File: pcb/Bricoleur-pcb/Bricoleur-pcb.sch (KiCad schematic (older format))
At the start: 29 parts, among them J1 USB_B_Micro, SW2 SW_Push, U11 SW_DP3T, U2 PYNQ-Shield-Bricoleur-pcb-cac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, U5 Arducam-OV5642, U6 Arducam-OV5642, U7 EFM32GG980, U8 UART_BOOT, U9 IP4220CZ6

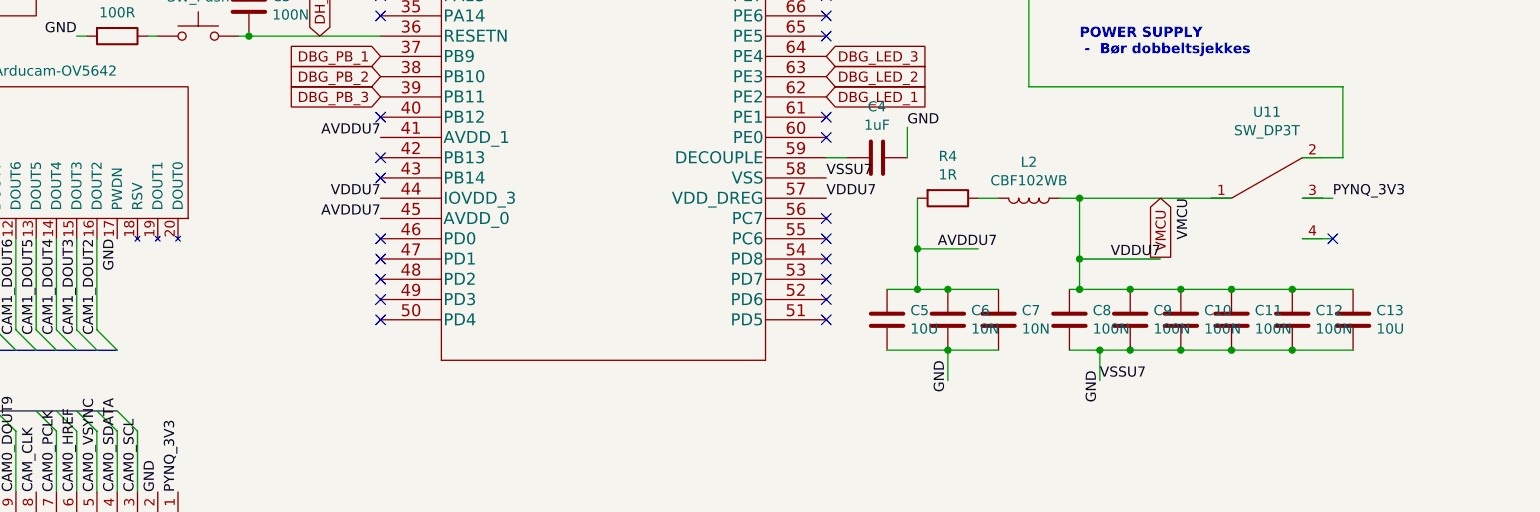
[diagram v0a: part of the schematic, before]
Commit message: Power and clock networks ready (probably).
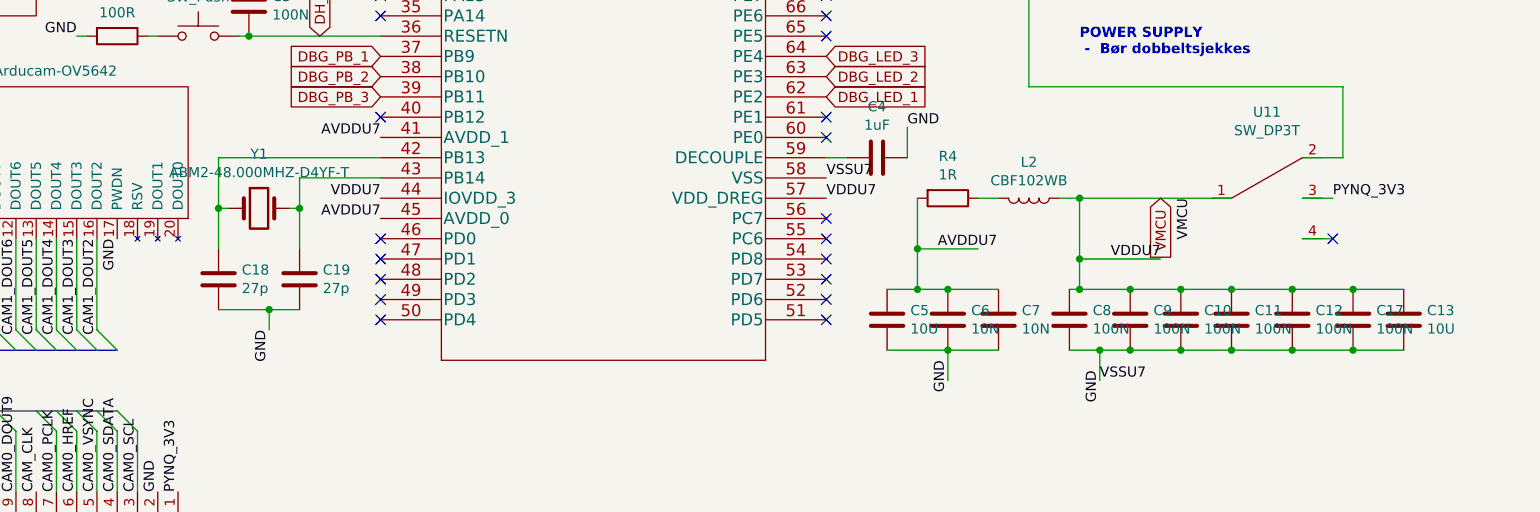
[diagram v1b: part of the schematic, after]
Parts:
- added C17: 100N, Capacitor_SMD:C_0402_1005Metric, symbol Device:C
- added C18, C19: 27p, Capacitor_SMD:C_0402_1005Metric, symbol Device:C
- added Y1: ABM2-48.000MHZ-D4YF-T, XTAL:XTAL, symbol Device:Crystal
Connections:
- net GND: now also C17.2, C18.2, C19.2
- net VMCU: now also C17.1
- net at U7.42 (PB13): now also C18.1, Y1.1
- net at U7.43 (PB14): now also C19.1, Y1.2
- no-connect marks 83 -> 81
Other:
- moved on the sheet: C13
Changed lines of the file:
@@
 L Device:C C13
 U 1 1 5BA5CA48
-P 10950 6100
-F 0 "C13" H 11065 6146 50  0000 L CNN
-F 1 "10U" H 11065 6055 50  0000 L CNN
-F 2 "Capacitor_SMD:C_0805_2012Metric" H 10988 5950 50  0001 C CNN
-F 3 "~" H 10950 6100 50  0001 C CNN
-	1    10950 6100
+P 11200 6100
+F 0 "C13" H 11315 6146 50  0000 L CNN
+F 1 "10U" H 11315 6055 50  0000 L CNN
+F 2 "Capacitor_SMD:C_0805_2012Metric" H 11238 5950 50  0001 C CNN
+F 3 "~" H 11200 6100 50  0001 C CNN
+	1    11200 6100
 	1    0    0    -1
 $EndComp
@@
 NoConn ~ 6150 4600
 NoConn ~ 6150 5100
-NoConn ~ 6150 5300
-NoConn ~ 6150 5400
 NoConn ~ 6150 5700
 NoConn ~ 6150 5800
@@
 Wire Wire Line
 	9750 2750 9300 2750
-Wire Wire Line
-	2350 5200 2950 5200
-Wire Wire Line
-	8350 4000 9050 4000
-Wire Wire Line
-	2350 5700 2950 5700
-Wire Bus Line
-	8950 2700 8950 4200
-Wire Bus Line
-	3000 650  3000 4750
-Wire Bus Line
-	3050 4750 3050 5650
-Wire Bus Line
-	2900 6550 4850 6550
-Wire Bus Line
-	2900 5100 2900 6550
-Wire Bus Line
-	3000 6250 4850 6250
-Wire Bus Line
-	2900 3600 2900 4850
 Text Label 10050 1750 0    50   ~ 0
 USB_D-
 Text Label 10050 1850 0    50   ~ 0
 USB_D+
+$Comp
+L Device:C C17
+U 1 1 5BB181A5
+P 10950 6100
+F 0 "C17" H 11065 6146 50  0000 L CNN
+F 1 "100N" H 11065 6055 50  0000 L CNN
+F 2 "Capacitor_SMD:C_0402_1005Metric" H 10988 5950 50  0001 C CNN
+F 3 "~" H 10950 6100 50  0001 C CNN
+	1    10950 6100
+	1    0    0    -1
+$EndComp
+Wire Wire Line
+	11200 5950 10950 5950
+Connection ~ 10950 5950
+Wire Wire Line
+	11200 6250 10950 6250
+Connection ~ 10950 6250
+$Comp
+L Device:Crystal Y1
+U 1 1 5BB326B9
+P 5550 5550
+F 0 "Y1" H 5550 5818 50  0000 C CNN
+F 1 "ABM2-48.000MHZ-D4YF-T" H 5550 5727 50  0000 C CNN
+F 2 "XTAL:XTAL" H 5550 5550 50  0001 C CNN
+F 3 "~" H 5550 5550 50  0001 C CNN
+	1    5550 5550
+	1    0    0    -1
+$EndComp
+Wire Wire Line
+	5750 5750 5750 5550
+Wire Wire Line
+	5750 5550 5700 5550
+Wire Wire Line
+	5350 5750 5350 5550
+Wire Wire Line
+	5350 5550 5400 5550
+Text Label 5600 6150 3    50   ~ 0
+GND
+Wire Wire Line
+	5600 6150 5600 6050
+Wire Wire Line
+	5600 6050 5350 6050
+Wire Wire Line
+	5600 6050 5750 6050
+Connection ~ 5600 6050
+Wire Wire Line
+	5750 5400 5750 5550
+Connection ~ 5750 5550
+Wire Wire Line
+	5350 5300 5350 5550
+Connection ~ 5350 5550
+$Comp
+L Device:C C18
+U 1 1 5BB1AE61
+P 5350 5900
+F 0 "C18" H 5465 5946 50  0000 L CNN
+F 1 "27p" H 5465 5855 50  0000 L CNN
+F 2 "Capacitor_SMD:C_0402_1005Metric" H 5388 5750 50  0001 C CNN
+F 3 "~" H 5350 5900 50  0001 C CNN
+	1    5350 5900
+	1    0    0    -1
+$EndComp
+$Comp
+L Device:C C19
+U 1 1 5BB1B027
+P 5750 5900
+F 0 "C19" H 5865 5946 50  0000 L CNN
+F 1 "27p" H 5865 5855 50  0000 L CNN
+F 2 "Capacitor_SMD:C_0402_1005Metric" H 5788 5750 50  0001 C CNN
+F 3 "~" H 5750 5900 50  0001 C CNN
+	1    5750 5900
+	1    0    0    -1
+$EndComp
+Wire Wire Line
+	6150 5400 5750 5400
+Wire Wire Line
+	5350 5300 6150 5300
+Wire Wire Line
+	2350 5700 2950 5700
+Wire Wire Line
+	8350 4000 9050 4000
+Wire Wire Line
+	2350 5200 2950 5200
+Wire Bus Line
+	8950 2700 8950 4200
+Wire Bus Line
+	3050 4750 3050 5650
+Wire Bus Line
+	3000 650  3000 4750
+Wire Bus Line
+	2900 6550 4850 6550
+Wire Bus Line
+	2900 5100 2900 6550
+Wire Bus Line
+	3000 6250 4850 6250
+Wire Bus Line
+	2900 3600 2900 4850
 $EndSCHEMATC

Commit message: Moar routing
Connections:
- net US0_CLK: now also U2.46 (IO4); no longer U2.43 (IO7)
- net US0_RX: now also U2.43 (IO7); no longer U2.46 (IO4)
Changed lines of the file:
@@
 Text Label 2350 5700 0    50   ~ 0
 US0_TX
+Text Label 2350 4900 0    50   ~ 0
+US0_RX
 Text Label 2350 5200 0    50   ~ 0
-US0_RX
-Text Label 2350 4900 0    50   ~ 0
 US0_CLK
 Entry Wire Line

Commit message: Overwrite
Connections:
- net CAM0_DOUT2: now also U2.57 (IO27); no longer U2.50 (IO0)
- net CAM0_DOUT3: now also U2.50 (IO0); no longer U2.58 (IO26)
- net CAM0_DOUT5: now also U2.58 (IO26); no longer U2.57 (IO27)
- net USB_D+: now also U9.3 (I/O); no longer U9.4 (I/O_3)
- net USB_R_D+: now reaches R2.1, U7.74 (PF10)
- net USB_R_D-: now reaches R3.2, U7.75 (PF11)
- net USB_5v: now reaches J1.1 (VBUS), L1.1, U9.5 (VP)
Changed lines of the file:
@@
 	10700 1850 9400 1850
-Wire Wire Line
-	9400 1850 9400 2650
 Wire Wire Line
 	9400 3700 8350 3700
@@
 Wire Wire Line
 	9600 3000 9600 2050
-Wire Wire Line
-	9750 2650 9400 2650
-Connection ~ 9400 2650
-Wire Wire Line
-	9400 2650 9400 3350
 Text Label 11100 1450 1    50   ~ 0
 GND
@@
 Text Label 4950 6950 1    50   ~ 0
 CAM0_SCL
+Text Label 2350 6300 0    50   ~ 0
+CAM0_DOUT2
 Text Label 2350 5600 0    50   ~ 0
-CAM0_DOUT2
-Text Label 2350 6400 0    50   ~ 0
 CAM0_DOUT3
 Text Label 2350 5500 0    50   ~ 0
 CAM0_DOUT4
-Text Label 2350 6300 0    50   ~ 0
+Text Label 2350 6400 0    50   ~ 0
 CAM0_DOUT5
 Text Label 2350 5400 0    50   ~ 0
@@
 Text GLabel 8350 3400 2    50   Input ~ 0
 DH_TDO_SWO
-NoConn ~ 9750 2450
 $Comp
 L Bricoleur-pcb-rescue:SW_DP3T-Bricoleur-pcb-cache U11
@@
 	5350 5300 6150 5300
 Wire Wire Line
+	9400 1850 9400 2450
+Wire Wire Line
+	9750 2450 9400 2450
+Connection ~ 9400 2450
+Wire Wire Line
+	9400 2450 9400 3350
+NoConn ~ 9750 2650
+Text Label 10000 2050 0    50   ~ 0
+USB_5v
+Text Label 8400 3700 0    50   ~ 0
+USB_R_D-
+Text Label 8400 3800 0    50   ~ 0
+USB_R_D+
+Wire Wire Line
+	2350 5200 2950 5200
+Wire Wire Line
+	8350 4000 9050 4000
+Wire Wire Line
 	2350 5700 2950 5700
-Wire Wire Line
-	8350 4000 9050 4000
-Wire Wire Line
-	2350 5200 2950 5200
 Wire Bus Line
 	8950 2700 8950 4200
 Wire Bus Line
+	3000 650  3000 4750
+Wire Bus Line
 	3050 4750 3050 5650
 Wire Bus Line
-	3000 650  3000 4750
-Wire Bus Line
 	2900 6550 4850 6550

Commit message: Layout finished.
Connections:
- net CAM0_DOUT2: now also U2.44 (IO6); no longer U2.57 (IO27)
- net CAM0_DOUT3: now also U2.53 (IO31); no longer U2.50 (IO0)
- net CAM0_DOUT4: now also U2.52 (IO32); no longer U2.49 (IO1)
- net CAM0_DOUT5: now also U2.45 (IO5); no longer U2.58 (IO26)
- net CAM0_DOUT6: now also U2.54 (IO30); no longer U2.48 (IO2)
- net CAM0_DOUT7: now also U2.47 (IO3); no longer U2.56 (IO28)
- net CAM0_DOUT8: now also U2.55 (IO29); no longer U2.47 (IO3)
- net CAM0_DOUT9: now also U2.48 (IO2); no longer U2.55 (IO29)
- net CAM0_HREF: now also U2.57 (IO27); no longer U2.45 (IO5)
- net CAM0_PCLK: now also U2.56 (IO28); no longer U2.54 (IO30)
- net CAM0_SCL: now also U2.50 (IO0); no longer U2.52 (IO32)
- net CAM0_SDATA: now also U2.58 (IO26); no longer U2.44 (IO6)
- net CAM0_VSYNC: now also U2.49 (IO1); no longer U2.53 (IO31)
- net CAM1_HREF: now also U2.36 (IO40); no longer U2.29 (IO13)
- net CAM1_VSYNC: now also U2.29 (IO13); no longer U2.36 (IO40)
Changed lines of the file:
@@
 Text Label 4950 6950 1    50   ~ 0
 CAM0_SCL
+Text Label 2350 5000 0    50   ~ 0
+CAM0_DOUT2
+Text Label 2350 5900 0    50   ~ 0
+CAM0_DOUT3
+Text Label 2350 5800 0    50   ~ 0
+CAM0_DOUT4
+Text Label 2350 5100 0    50   ~ 0
+CAM0_DOUT5
+Text Label 2350 6000 0    50   ~ 0
+CAM0_DOUT6
+Text Label 2350 5300 0    50   ~ 0
+CAM0_DOUT7
+Text Label 2350 6100 0    50   ~ 0
+CAM0_DOUT8
+Text Label 2350 5400 0    50   ~ 0
+CAM0_DOUT9
+Text Label 2350 6200 0    50   ~ 0
+CAM0_PCLK
 Text Label 2350 6300 0    50   ~ 0
-CAM0_DOUT2
-Text Label 2350 5600 0    50   ~ 0
-CAM0_DOUT3
-Text Label 2350 5500 0    50   ~ 0
-CAM0_DOUT4
-Text Label 2350 6400 0    50   ~ 0
-CAM0_DOUT5
-Text Label 2350 5400 0    50   ~ 0
-CAM0_DOUT6
-Text Label 2350 6200 0    50   ~ 0
-CAM0_DOUT7
-Text Label 2350 5300 0    50   ~ 0
-CAM0_DOUT8
-Text Label 2350 6100 0    50   ~ 0
-CAM0_DOUT9
-Text Label 2350 6000 0    50   ~ 0
-CAM0_PCLK
-Text Label 2350 5100 0    50   ~ 0
 CAM0_HREF
 Entry Wire Line
@@
 Entry Wire Line
 	2800 5300 2900 5400
-Text Label 2350 5900 0    50   ~ 0
+Text Label 2350 5500 0    50   ~ 0
 CAM0_VSYNC
-Text Label 2350 5000 0    50   ~ 0
+Text Label 2350 6400 0    50   ~ 0
 CAM0_SDATA
-Text Label 2350 5800 0    50   ~ 0
+Text Label 2350 5600 0    50   ~ 0
 CAM0_SCL
 Entry Wire Line
@@
 Text Label 2350 4300 0    50   ~ 0
 CAM1_PCLK
+Text Label 2350 4200 0    50   ~ 0
+CAM1_HREF
 Text Label 2350 3500 0    50   ~ 0
-CAM1_HREF
-Text Label 2350 4200 0    50   ~ 0
 CAM1_VSYNC
 Text Label 2350 3300 0    50   ~ 0

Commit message: Cleanup, labeling, schematic size reduction
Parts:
- added D10, D8, D9: BAT54S, Package_TO_SOT_SMD:SOT-23, symbol Diode:BAT54S
- U2: value PYNQ-Shield-Bricoleur-pcb-cache -> PYNQ-Shield-(Arduino)
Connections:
- net DH_TCK_SWCLK: now also D10.3
- net GND: now also D10.1, D8.1, D9.1
- net VMCU: now also D10.2, D8.2, D9.2
- net Sheet5BB71F0E/INP renamed MCU_BOOT_RX
- net MCU_BOOT_RX: now also D8.3
- net sheet5BB7B6EA/INP renamed MCU_BOOT_TX
- net MCU_BOOT_TX: now also D9.3
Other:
- note added: "POWER SUPPLY\n\n"
- note removed: "POWER SUPPLY\n - Bør dobbeltsjekkes \n"
- moved on the sheet: C10, C11, C12, C13, C17, C5, C6, C7, C8, C9
